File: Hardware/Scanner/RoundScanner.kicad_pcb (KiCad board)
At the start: 4 copper layers, 45 x 42.5 mm, 78 parts, among them J1 I2C ThroughHole, J3 I2C, J4 Interface, Q1 BSS138DW-7-F, U1 OPA2376xxD, U2 NAU7802SGI, U4 OPA2376xxD, U5 TLC59208FIPWR, U6 AS7341-DLGT, U7 AP7312-1833W6-7, X1 4.9152 MHz

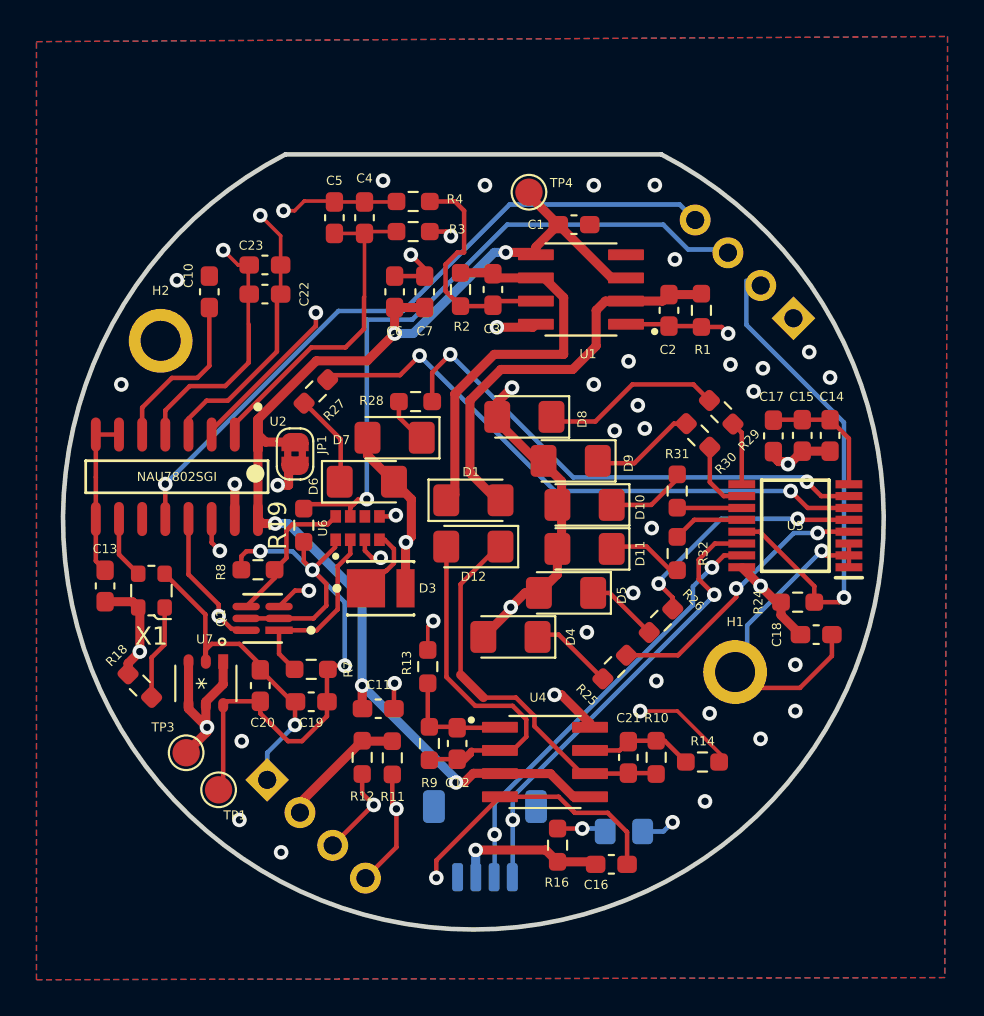
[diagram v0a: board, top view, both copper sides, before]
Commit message: Initial conversion and cleanup from a feather to an esp32s3
added USB power
Added switching 3.6-5v regulator
updated schematic ground to use built in kicad libraries
updated partially broken library references to eagle lib files
added circuit simulator of trigger and wakeup simulation

Signed-off-by: lokimetasmith <lokimail@gmail.com>
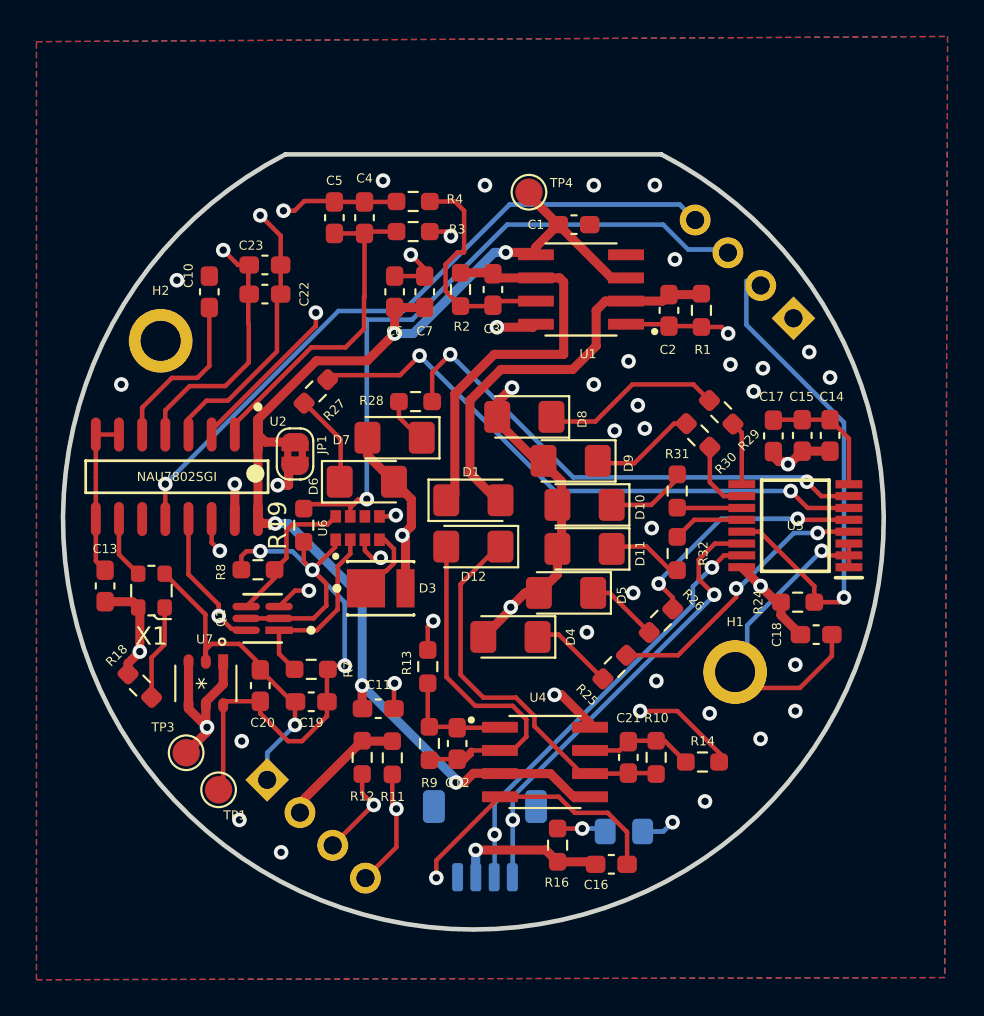
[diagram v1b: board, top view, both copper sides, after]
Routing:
- net +3V3: track 159.5 -> 160.0 mm

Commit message: added footprint for MTSM2601SMF1-100
Signed-off-by: lokimetasmith <lokimail@gmail.com>
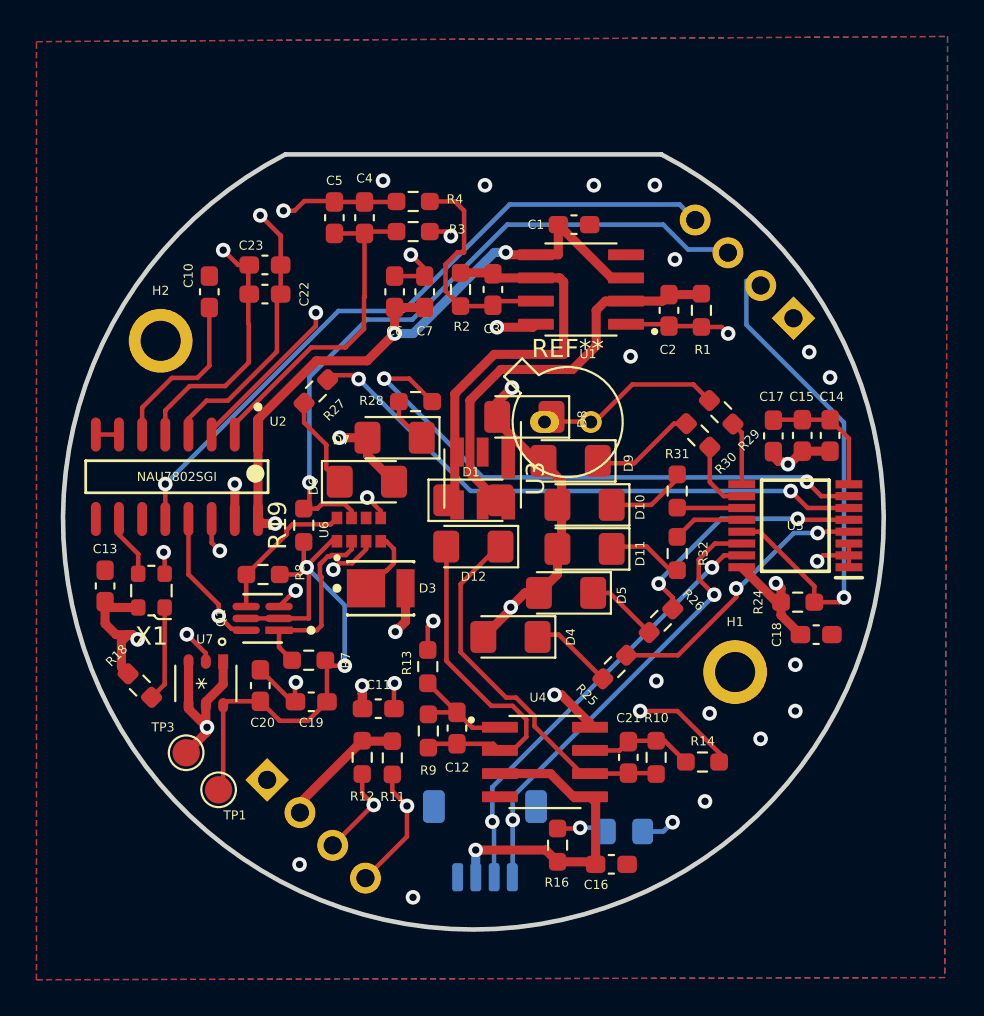
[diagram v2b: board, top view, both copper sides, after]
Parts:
- removed JP1: Jumper_2_Bridged, Jumper:SolderJumper-2_P1.3mm_Bridged2Bar_RoundedPad1.0x1.5mm
- removed TP4: Test_2.5V, TestPoint:TestPoint_Pad_D1.5mm
- added REF**: TO-46-2_Window, Package_TO_SOT_THT:TO-46-2_Window, F.Cu at (93.2, 102.0)
- added U3: ~, MTSM2601SMF1-100:MTSM2601SMF1-100, F.Cu at (89.8, 105.1)
- moved C12 0.85 mm to (88.4, 118.8)
- moved R9 0.69 mm to (86.8, 118.9)
- moved R7 0.52 mm to (80.3, 115.1)
- moved R8 0.38 mm to (77.8, 110.4), turned to 180 degrees
- moved U6 0.11 mm to (83.0, 107.9)
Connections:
- net AS7341_INT renamed /MCU + IO/AS7341_INT
- net DRDY_INT renamed /ADC/DRDY_INT
- net Net-(C2-Pad1) renamed /InGaS Sensor/Anode
- net Net-(C3-Pad1) renamed /InGaS Sensor/Cathode
- net SCL_2v renamed /MCU + IO/SCL_2v
- net SDA_2v renamed /MCU + IO/SDA_2v
- C1 pad 2: +2V5 -> +3V3
- C11 pad 2: +2V5 -> +3V3
- C6 pad 2: +2V5 -> +3V3
- C7 pad 2: +2V5 -> +3V3
- J3 pad MP: (no net) -> GND
- J4 pad 2: LED RESET -> /Power/LED RESET
- U1 pad 3: +2V5 -> +3V3
- U1 pad 5: +2V5 -> +3V3
- U2 pad 1: +2V5 -> +3V3
- U2 pad 16: +2V5 -> +3V3
- U4 pad 3: +2V5 -> +3V3
- U4 pad 5: +2V5 -> +3V3
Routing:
- net +2V5: track 68.3 -> 0.00 mm, vias 5 -> 0
- net GND: track 73.1 -> 28.6 mm, vias 37 -> 25
- net +3V3: track 160.0 -> 125.9 mm, vias 12 -> 16
- net +1V8: track 37.5 -> 31.8 mm, vias 3 -> 2
- net Net-(R28-Pad1): track 28.1 -> 31.3 mm
- net SDA: track 64.9 -> 62.5 mm
- net Net-(D12-A): track 20.1 -> 18.9 mm
- net Net-(R27-Pad1): track 32.2 -> 31.4 mm
- net Net-(D12-K): track 20.8 -> 20.1 mm
- net /ADC/AIN2+: track 59.6 -> 60.3 mm
- net SCL: track 60.6 -> 61.2 mm
